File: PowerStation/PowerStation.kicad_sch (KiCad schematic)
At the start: 0 parts

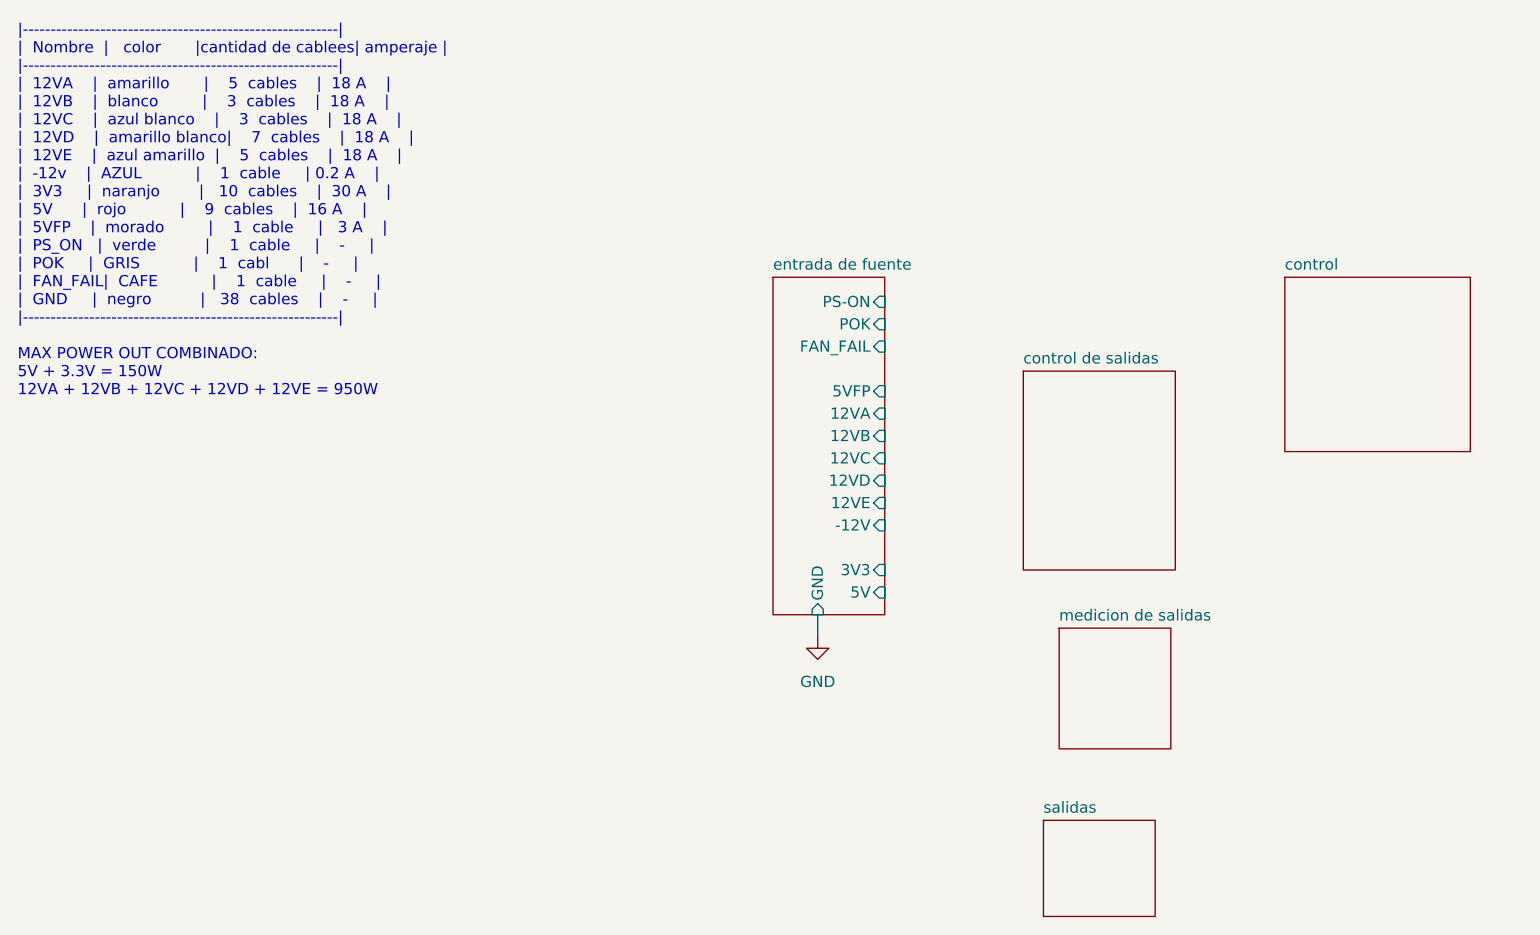
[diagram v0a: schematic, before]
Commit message: terminando diagrama
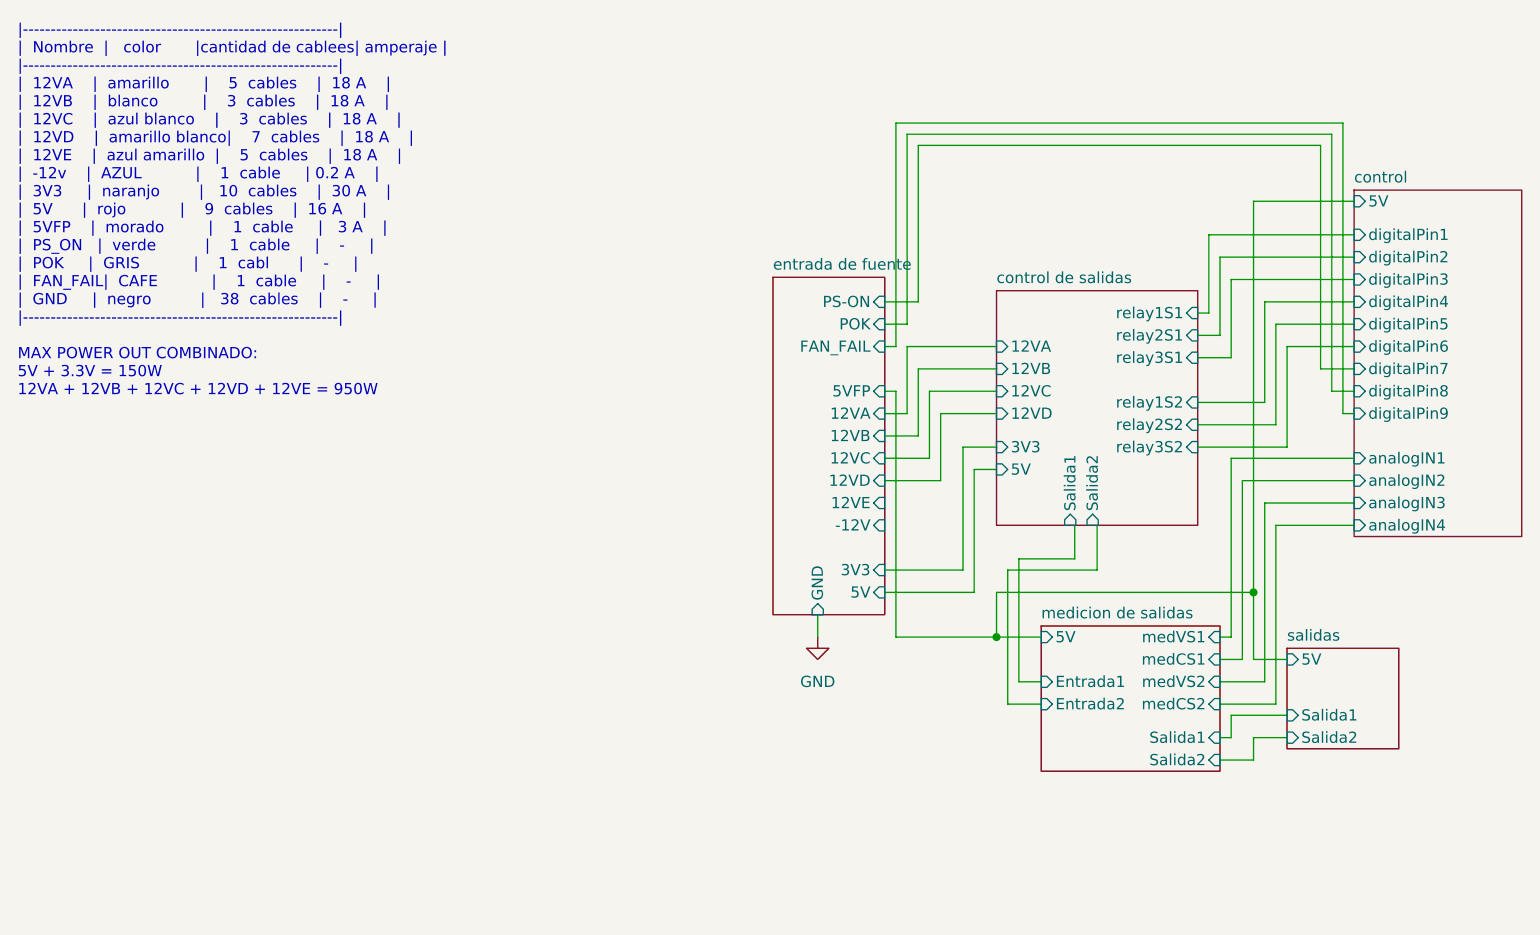
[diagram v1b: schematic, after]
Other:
- sheet control ports: added 5V, analogIN1, analogIN2, analogIN3, analogIN4, digitalPin1, digitalPin2, digitalPin3, digitalPin4, digitalPin5, digitalPin6, digitalPin7, digitalPin8, digitalPin9; removed none
- sheet control de salidas ports: added 12VA, 12VB, 12VC, 12VD, 3V3, 5V, Salida1, Salida2, relay1S1, relay1S2, relay2S1, relay2S2, relay3S1, relay3S2; removed none
- sheet medicion de salidas ports: added 5V, Entrada1, Entrada2, Salida1, Salida2, medCS1, medCS2, medVS1, medVS2; removed none
- sheet salidas ports: added 5V, Salida1, Salida2; removed none
